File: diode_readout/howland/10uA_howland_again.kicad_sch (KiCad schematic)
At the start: 15 parts, among them J3 MMCX-KE-STM, U5 INA826, U6 AD8628

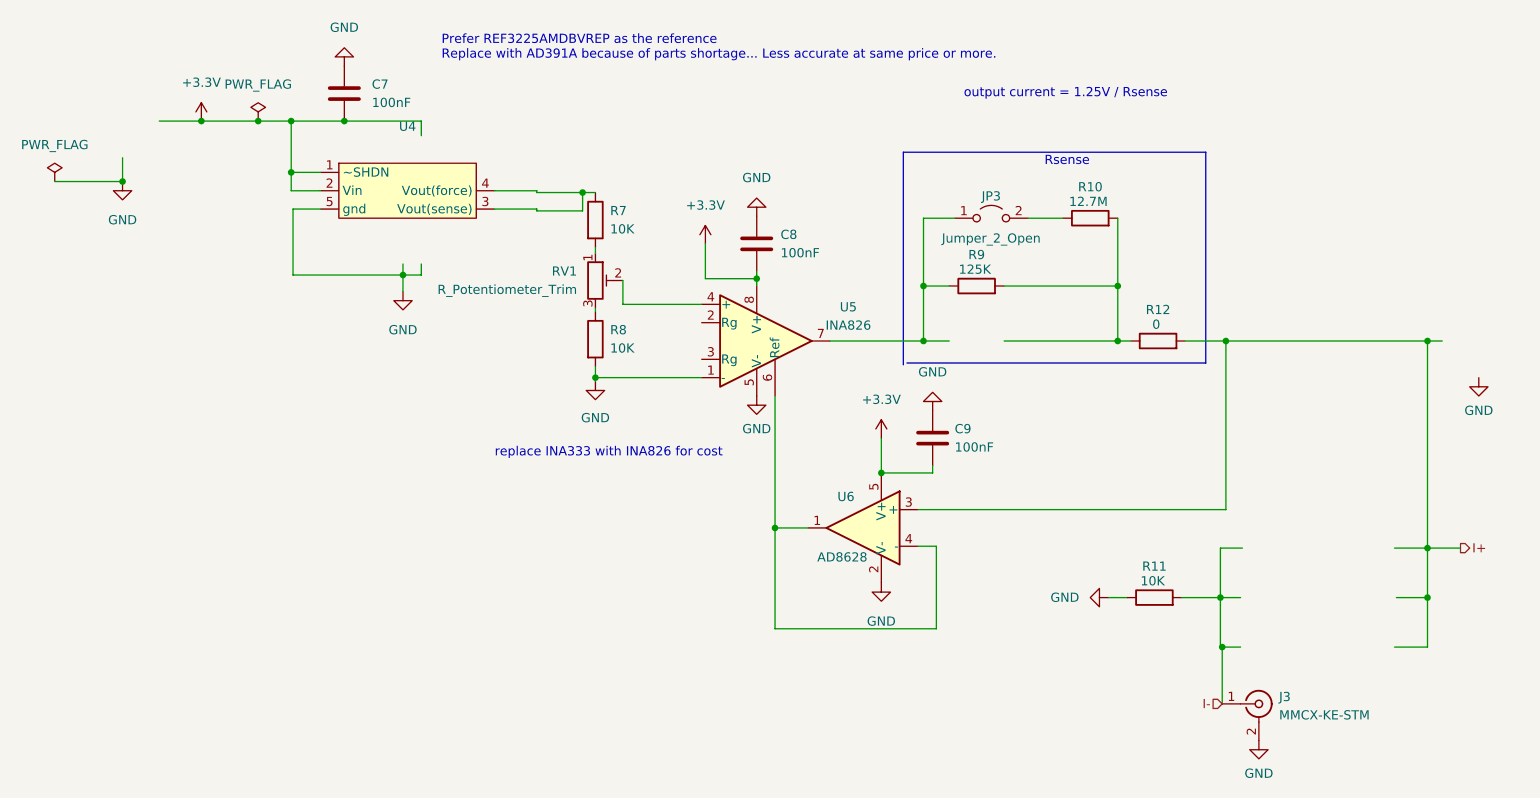
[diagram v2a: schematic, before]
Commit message: tweak 10K resistors because of parts shortages
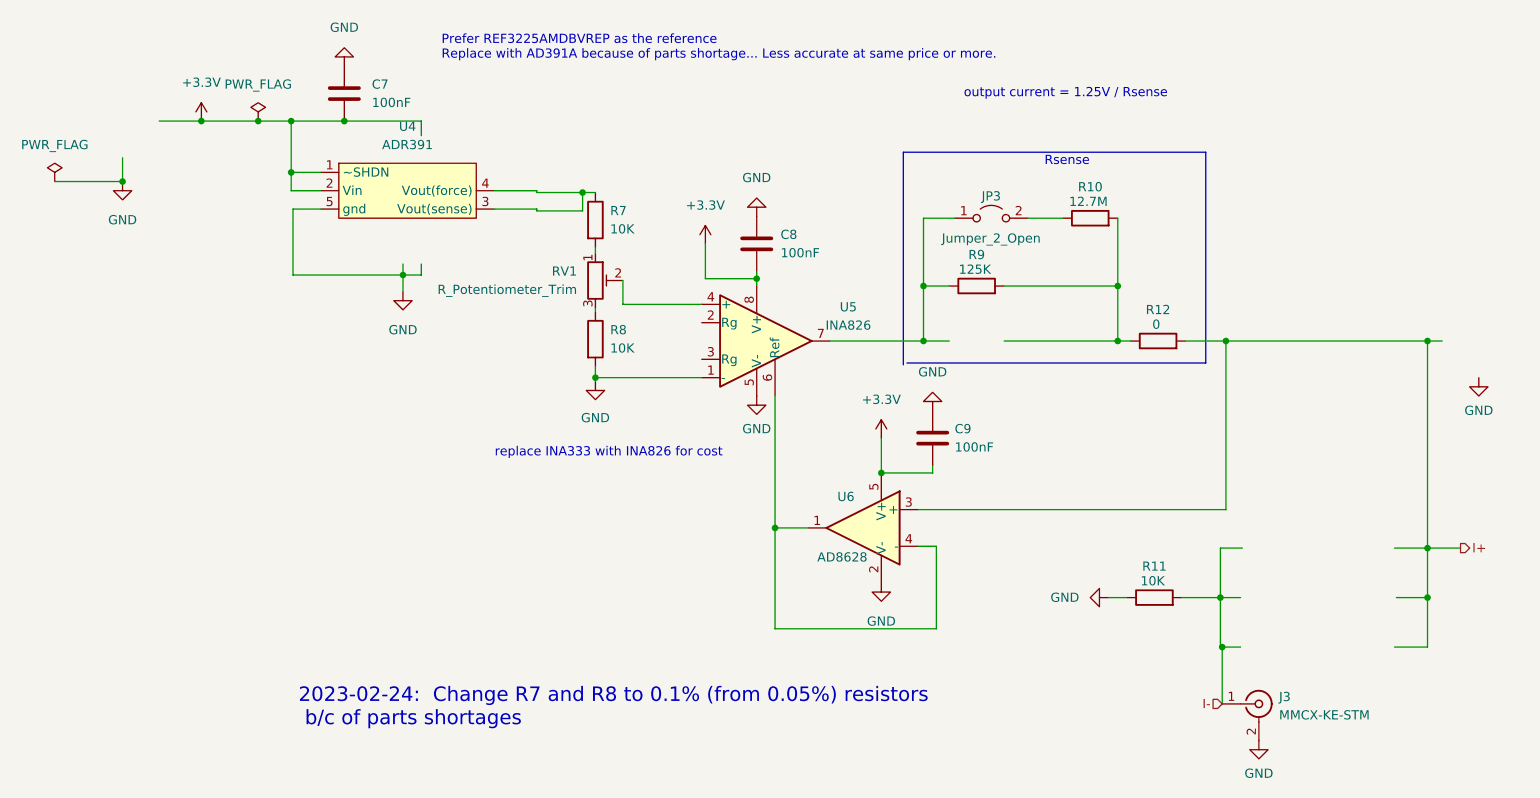
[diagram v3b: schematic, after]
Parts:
- U4: value (none) -> ADR391; footprint (none) -> Package_TO_SOT_SMD:TSOT-23-5_HandSoldering
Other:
- note added: "2023-02-24: Change R7 and R8 to 0.1% (from 0.05%) resistors b/c of parts shortages"
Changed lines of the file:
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@@
     (effects (font (size 1.27 1.27)) (justify left bottom))
+  )
+  (text "2023-02-24:  Change R7 and R8 to 0.1% (from 0.05%) resistors\n b/c of parts shortages"
+    (at 68.58 137.922 0)
+    (effects (font (size 2 2)) (justify left bottom))
   )
   (hierarchical_label "I+" (shape output) (at 229.616 113.03 0)
@@
     (in_bom yes) (on_board yes) (fields_autoplaced)
     (property "Reference" "U4" (id 0) (at 83.693 54.61 0))
-    (property "Value" "" (id 1) (at 83.693 57.15 0))
-    (property "Footprint" "" (id 2) (at 75.438 64.77 0)
+    (property "Value" "ADR391" (id 1) (at 83.693 57.15 0))
+    (property "Footprint" "Package_TO_SOT_SMD:TSOT-23-5_HandSoldering" (id 2) (at 75.438 64.77 0)
       (effects (font (size 1.27 1.27)) hide)
     )

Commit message: Add tweaks to diode readout
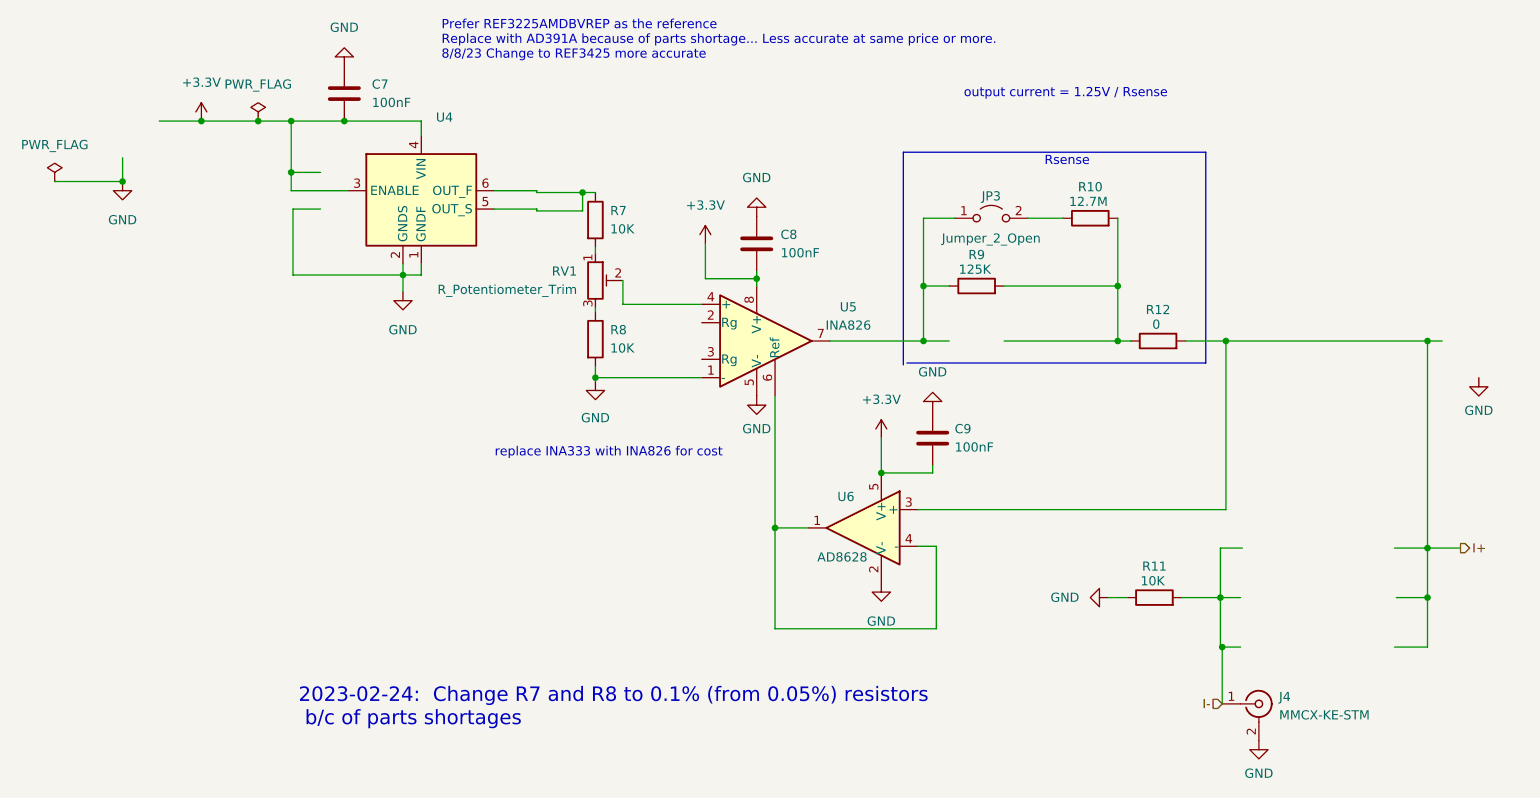
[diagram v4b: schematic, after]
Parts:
- removed U4: ADR391, Package_TO_SOT_SMD:TSOT-23-5_HandSoldering, symbol 0JLC-6:ADR391
- added U4: (no value), symbol Reference_Voltage:REF3225AMDBVREP
- renumbered J3 to J4
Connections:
- net +3V3: now also U4.3 (ENABLE), U4.4 (VIN)
- net GND: now also U4.1 (GNDF), U4.2 (GNDS)
- net at R7.1: now also U4.5 (OUT_S), U4.6 (OUT_F)
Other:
- note added: "Prefer REF3225AMDBVREP as the reference Replace with AD391A because of parts shortage... Less accurate at same price or more. 8/8/23 Change to REF3425 more accurate"
- note removed: "Prefer REF3225AMDBVREP as the reference Replace with AD391A because of parts shortage... Less accurate at same price or more."
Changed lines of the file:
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@@
     (stroke (width 0) (type default) (color 0 0 0 0))
   )
-  (wire (pts (xy 67.564 63.5) (xy 71.628 63.5))
+  (wire (pts (xy 67.564 63.5) (xy 75.438 63.5))
     (stroke (width 0) (type default) (color 0 0 0 0))
   )
@@
     (effects (font (size 1.27 1.27)) (justify left bottom))
   )
-  (text "Prefer REF3225AMDBVREP as the reference\nReplace with AD391A because of parts shortage... Less accurate at same price or more."
+  (text "Prefer REF3225AMDBVREP as the reference\nReplace with AD391A because of parts shortage... Less accurate at same price or more.\n8/8/23 Change to REF3425 more accurate"
     (at 88.392 45.466 0)
     (effects (font (size 1.27 1.27)) (justify left bottom))
@@
   (symbol (lib_id "power:GND") (at 132.08 67.056 180) (unit 1)
     (in_bom yes) (on_board yes) (fields_autoplaced)
-    (property "Reference" "#PWR019" (id 0) (at 132.08 60.706 0)
+    (property "Reference" "#PWR020" (id 0) (at 132.08 60.706 0)
       (effects (font (size 1.27 1.27)) hide)
     )
@@
   (symbol (lib_id "power:+3.3V") (at 149.352 97.79 0) (unit 1)
     (in_bom yes) (on_board yes) (fields_autoplaced)
-    (property "Reference" "#PWR021" (id 0) (at 149.352 101.6 0)
+    (property "Reference" "#PWR022" (id 0) (at 149.352 101.6 0)
       (effects (font (size 1.27 1.27)) hide)
     )
@@
     (pin "2")
   )
-  (symbol (lib_id "0JLC-6:ADR391") (at 84.328 64.77 0) (unit 1)
-    (in_bom yes) (on_board yes) (fields_autoplaced)
-    (property "Reference" "U4" (id 0) (at 83.693 54.61 0))
-    (property "Value" "ADR391" (id 1) (at 83.693 57.15 0))
-    (property "Footprint" "Package_TO_SOT_SMD:TSOT-23-5_HandSoldering" (id 2) (at 75.438 64.77 0)
-      (effects (font (size 1.27 1.27)) hide)
-    )
-    (property "Datasheet" "" (id 3) (at 75.438 64.77 0)
-      (effects (font (size 1.27 1.27)) hide)
-    )
-    (property "LCSC" "C141376" (id 4) (at 81.788 64.77 0)
-      (effects (font (size 1.27 1.27)) hide)
-    )
-    (property "MPN" "ADR391AUJZ-REEL7 " (id 5) (at 81.788 64.77 0)
-      (effects (font (size 1.27 1.27)) hide)
-    )
-    (pin "1")
-    (pin "2")
-    (pin "3")
-    (pin "4")
-    (pin "5")
-  )
   (symbol (lib_id "power:+3.3V") (at 124.968 70.866 0) (unit 1)
     (in_bom yes) (on_board yes) (fields_autoplaced)
-    (property "Reference" "#PWR018" (id 0) (at 124.968 74.676 0)
+    (property "Reference" "#PWR019" (id 0) (at 124.968 74.676 0)
       (effects (font (size 1.27 1.27)) hide)
     )
@@
   (symbol (lib_id "power:GND") (at 180.848 119.888 270) (unit 1)
     (in_bom yes) (on_board yes) (fields_autoplaced)
-    (property "Reference" "#PWR024" (id 0) (at 174.498 119.888 0)
+    (property "Reference" "#PWR025" (id 0) (at 174.498 119.888 0)
       (effects (font (size 1.27 1.27)) hide)
     )
@@
     (pin "2")
   )
+  (symbol (lib_id "Reference_Voltage:REF3225AMDBVREP") (at 85.598 63.5 0) (unit 1)
+    (in_bom yes) (on_board yes) (fields_autoplaced)
+    (property "Reference" "U4" (id 0) (at 87.6174 53.34 0)
+      (effects (font (size 1.27 1.27)) (justify left))
+    )
+    (property "Value" "" (id 1) (at 87.6174 55.88 0)
+      (effects (font (size 1.27 1.27) italic) (justify left))
+    )
+    (property "Footprint" "" (id 2) (at 87.503 73.025 0)
+      (effects (font (size 1.27 1.27) italic) (justify left) hide)
+    )
+    (property "Datasheet" "http://www.ti.com/lit/ds/symlink/ref3240-ep.pdf" (id 3) (at 85.598 62.23 0)
+      (effects (font (size 1.27 1.27) italic) hide)
+    )
+    (property "LCSC" "C187836" (id 4) (at 85.598 63.5 0)
+      (effects (font (size 1.27 1.27)) hide)
+    )
+    (pin "1")
+    (pin "2")
+    (pin "3")
+    (pin "4")
+    (pin "5")
+    (pin "6")
+  )
   (symbol (lib_id "power:GND") (at 44.196 62.23 0) (unit 1)
     (in_bom yes) (on_board yes) (fields_autoplaced)
-    (property "Reference" "#PWR013" (id 0) (at 44.196 68.58 0)
+    (property "Reference" "#PWR014" (id 0) (at 44.196 68.58 0)
       (effects (font (size 1.27 1.27)) hide)
     )
@@
   (symbol (lib_id "power:GND") (at 149.352 117.856 0) (unit 1)
     (in_bom yes) (on_board yes) (fields_autoplaced)
-    (property "Reference" "#PWR022" (id 0) (at 149.352 124.206 0)
+    (property "Reference" "#PWR023" (id 0) (at 149.352 124.206 0)
       (effects (font (size 1.27 1.27)) hide)
     )
@@
   (symbol (lib_id "power:GND") (at 83.058 77.47 0) (unit 1)
     (in_bom yes) (on_board yes) (fields_autoplaced)
-    (property "Reference" "#PWR016" (id 0) (at 83.058 83.82 0)
+    (property "Reference" "#PWR017" (id 0) (at 83.058 83.82 0)
       (effects (font (size 1.27 1.27)) hide)
     )
@@
   (symbol (lib_id "power:GND") (at 156.464 93.98 180) (unit 1)
     (in_bom yes) (on_board yes) (fields_autoplaced)
-    (property "Reference" "#PWR023" (id 0) (at 156.464 87.63 0)
+    (property "Reference" "#PWR024" (id 0) (at 156.464 87.63 0)
       (effects (font (size 1.27 1.27)) hide)
     )
@@
   (symbol (lib_id "0JLC-6:MMCX-KE-STM") (at 201.676 134.62 0) (unit 1)
     (in_bom yes) (on_board yes) (fields_autoplaced)
-    (property "Reference" "J3" (id 0) (at 204.47 133.6431 0)
+    (property "Reference" "J4" (id 0) (at 204.47 133.6431 0)
       (effects (font (size 1.27 1.27)) (justify left))
     )
@@
   (symbol (lib_id "power:GND") (at 232.156 89.408 0) (unit 1)
     (in_bom yes) (on_board yes) (fields_autoplaced)
-    (property "Reference" "#PWR026" (id 0) (at 232.156 95.758 0)
+    (property "Reference" "#PWR027" (id 0) (at 232.156 95.758 0)
       (effects (font (size 1.27 1.27)) hide)
     )
@@
   (symbol (lib_id "power:GND") (at 109.728 89.916 0) (unit 1)
     (in_bom yes) (on_board yes) (fields_autoplaced)
-    (property "Reference" "#PWR017" (id 0) (at 109.728 96.266 0)
+    (property "Reference" "#PWR018" (id 0) (at 109.728 96.266 0)
       (effects (font (size 1.27 1.27)) hide)
     )
@@
   (symbol (lib_id "power:GND") (at 132.08 91.948 0) (unit 1)
     (in_bom yes) (on_board yes) (fields_autoplaced)
-    (property "Reference" "#PWR020" (id 0) (at 132.08 98.298 0)
+    (property "Reference" "#PWR021" (id 0) (at 132.08 98.298 0)
       (effects (font (size 1.27 1.27)) hide)
     )
@@
   (symbol (lib_id "power:GND") (at 74.93 46.228 180) (unit 1)
     (in_bom yes) (on_board yes) (fields_autoplaced)
-    (property "Reference" "#PWR015" (id 0) (at 74.93 39.878 0)
+    (property "Reference" "#PWR016" (id 0) (at 74.93 39.878 0)
       (effects (font (size 1.27 1.27)) hide)
     )
@@
   (symbol (lib_id "power:GND") (at 201.676 139.7 0) (unit 1)
     (in_bom yes) (on_board yes) (fields_autoplaced)
-    (property "Reference" "#PWR025" (id 0) (at 201.676 146.05 0)
+    (property "Reference" "#PWR026" (id 0) (at 201.676 146.05 0)
       (effects (font (size 1.27 1.27)) hide)
     )
@@
   (symbol (lib_id "power:+3.3V") (at 55.118 53.848 0) (unit 1)
     (in_bom yes) (on_board yes) (fields_autoplaced)
-    (property "Reference" "#PWR014" (id 0) (at 55.118 57.658 0)
-      (effects (font (size 1.27 1.27)) hide)
-    )
+    (property "Reference" "#PWR015" (id 0) (at 55.118 57.658 0)
+      (effects (font (size 1.27 1.27)) hide)
+    )
